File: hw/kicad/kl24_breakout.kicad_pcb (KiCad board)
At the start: 2 copper layers, 36.1 x 20.8 mm, 56 parts, among them J1 USB-micro-ab, J2 ARM_10PIN, P1 BATT+, P10 TST, P11 TST, P12 TST, P13 TST, P14 TST, P15 TST, P16 TST, P17 TST, P18 TST, P19 TST, P2 BATT-, P20 TST, P21 TST, P22 TST, P23 TST, P24 TST, P25 TST, P26 TST, P27 TST, P28 TST, P29 TST, P3 USB_V, P30 TST, P31 TST, P32 TST, P33 TST, P34 TST, P35 TST, P36 TST, P4 USB_GND, P5 TST, P6 TST, P7 TST, P8 TST, P9 TST, U1 MCP73831, U2 M25P05-A, U3 MKL24Z64VFM4, U4 LP3985, X1 CRYSTAL

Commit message: - add indicator led + resitor and jumper to pcb
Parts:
- added D3: LED, LED-0603, F.Cu at (150.2, 79.6)
- added JP1: JUMPER, jmp_small, F.Cu at (154.1, 82.2)
- added R5: 330, SM0603, F.Cu at (153.7, 77.0)
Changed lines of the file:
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@@
-(kicad_pcb (version 3) (host pcbnew "(2013-03-31 BZR 4008)-stable")
+(kicad_pcb (version 3) (host pcbnew "(2013-03-04 BZR 3984)-stable")
   (general
-    (links 88)
-    (no_connects 88)
+    (links 92)
+    (no_connects 92)
     (area 103.65685 49.41885 161.729444 95.639)
     (thickness 1.6)
@@
     (tracks 0)
     (zones 0)
-    (modules 56)
-    (nets 39)
+    (modules 59)
+    (nets 41)
   )
   (page A3)
@@
   (net 31 9)
   (net 32 LIPO+)
-  (net 33 N-0000044)
-  (net 34 N-0000045)
+  (net 33 N-0000043)
+  (net 34 N-0000044)
   (net 35 N-0000046)
-  (net 36 USB_DM)
-  (net 37 USB_DP)
-  (net 38 USB_VBUS)
+  (net 36 N-0000047)
+  (net 37 N-0000048)
+  (net 38 USB_DM)
+  (net 39 USB_DP)
+  (net 40 USB_VBUS)
   (net_class Default "This is the default net class."
     (clearance 0.254)
@@
     (add_net 9)
     (add_net LIPO+)
+    (add_net N-0000043)
     (add_net N-0000044)
-    (add_net N-0000045)
     (add_net N-0000046)
+    (add_net N-0000047)
+    (add_net N-0000048)
     (add_net USB_DM)
     (add_net USB_DP)
@@
     (pad 1 thru_hole circle (at 0 0) (size 1.75 1.75) (drill 1.02)
       (layers *.Cu *.Mask F.SilkS)
-      (net 38 USB_VBUS)
+      (net 40 USB_VBUS)
     )
   )
@@
     (pad 1 smd rect (at -0.762 0) (size 0.635 1.143)
       (layers F.Cu F.Paste F.Mask)
-      (net 33 N-0000044)
+      (net 35 N-0000046)
     )
     (pad 2 smd rect (at 0.762 0) (size 0.635 1.143)
@@
     (pad 1 smd rect (at -0.762 0) (size 0.635 1.143)
       (layers F.Cu F.Paste F.Mask)
-      (net 35 N-0000046)
+      (net 37 N-0000048)
     )
     (pad 2 smd rect (at 0.762 0) (size 0.635 1.143)
       (layers F.Cu F.Paste F.Mask)
-      (net 34 N-0000045)
+      (net 36 N-0000047)
     )
     (model smd\resistors\R0603.wrl
@@
     (pad 1 smd rect (at -0.762 0) (size 0.635 1.143)
       (layers F.Cu F.Paste F.Mask)
-      (net 37 USB_DP)
+      (net 39 USB_DP)
     )
     (pad 2 smd rect (at 0.762 0) (size 0.635 1.143)
@@
     (pad 1 smd rect (at -0.762 0) (size 0.635 1.143)
       (layers F.Cu F.Paste F.Mask)
-      (net 36 USB_DM)
+      (net 38 USB_DM)
     )
     (pad 2 smd rect (at 0.762 0) (size 0.635 1.143)
@@
     (pad 1 smd rect (at -0.762 0) (size 0.635 1.143)
       (layers F.Cu F.Paste F.Mask)
-      (net 38 USB_VBUS)
+      (net 40 USB_VBUS)
     )
     (pad 2 smd rect (at 0.762 0) (size 0.635 1.143)
@@
     (pad 1 smd rect (at -0.762 0) (size 0.635 1.143)
       (layers F.Cu F.Paste F.Mask)
-      (net 38 USB_VBUS)
+      (net 40 USB_VBUS)
     )
     (pad 2 smd rect (at 0.762 0) (size 0.635 1.143)
@@
     (pad 1 smd rect (at -0.762 0) (size 0.635 1.143)
       (layers F.Cu F.Paste F.Mask)
-      (net 38 USB_VBUS)
+      (net 40 USB_VBUS)
     )
     (pad 2 smd rect (at 0.762 0) (size 0.635 1.143)
       (layers F.Cu F.Paste F.Mask)
-      (net 35 N-0000046)
+      (net 37 N-0000048)
     )
     (model smd\resistors\R0603.wrl
@@
     (pad 2 smd rect (at 0.762 0) (size 0.635 1.143)
       (layers F.Cu F.Paste F.Mask)
-      (net 38 USB_VBUS)
+      (net 40 USB_VBUS)
     )
     (model smd\resistors\R0603.wrl
@@
     (pad 1 smd rect (at 0 0) (size 0.55 1)
       (layers F.Cu F.Paste F.Mask)
-      (net 34 N-0000045)
+      (net 36 N-0000047)
     )
     (pad 2 smd rect (at 0.95 0) (size 0.55 1)
@@
     (pad 4 smd rect (at 1.9 -2.7) (size 0.55 1)
       (layers F.Cu F.Paste F.Mask)
-      (net 38 USB_VBUS)
+      (net 40 USB_VBUS)
     )
     (pad 5 smd rect (at 0 -2.7) (size 0.55 1)
       (layers F.Cu F.Paste F.Mask)
-      (net 33 N-0000044)
+      (net 35 N-0000046)
     )
   )
@@
     (pad 1 smd rect (at 0 0) (size 0.6 1.1)
       (layers F.Cu F.Paste F.Mask)
-      (net 38 USB_VBUS)
+      (net 40 USB_VBUS)
     )
     (pad 2 smd rect (at 0.95 0) (size 0.6 1.1)
@@
     (pad 3 smd rect (at 1.9 0) (size 0.6 1.1)
       (layers F.Cu F.Paste F.Mask)
-      (net 38 USB_VBUS)
+      (net 40 USB_VBUS)
     )
     (pad 4 smd rect (at 1.9 -2.8) (size 0.6 1.1)
@@
     (pad 1 smd rect (at -1.3 -2.85 270) (size 0.4 1.4)
       (layers F.Cu F.Paste F.Mask)
-      (net 38 USB_VBUS)
+      (net 40 USB_VBUS)
     )
     (pad 2 smd rect (at -0.65 -2.85 270) (size 0.4 1.4)
       (layers F.Cu F.Paste F.Mask)
-      (net 36 USB_DM)
+      (net 38 USB_DM)
     )
     (pad 3 smd rect (at 0 -2.85 270) (size 0.4 1.4)
       (layers F.Cu F.Paste F.Mask)
-      (net 37 USB_DP)
+      (net 39 USB_DP)
     )
     (pad 4 smd rect (at 0.65 -2.85 270) (size 0.4 1.4)
@@
     )
   )
+  (module SM0603 (layer F.Cu)
+    (at 153.67 76.962)
+    (attr smd)
+    (fp_text reference R5 (at 0 0) (layer F.SilkS)
+      (effects (font (size 0.508 0.4572) (thickness 0.1143)))
+    )
+    (fp_text value 330 (at 0 0) (layer F.SilkS) hide
+      (effects (font (size 0.508 0.4572) (thickness 0.1143)))
+    )
+    (fp_line (start -1.143 -0.635) (end 1.143 -0.635) (layer F.SilkS) (width 0.127))
+    (fp_line (start 1.143 -0.635) (end 1.143 0.635) (layer F.SilkS) (width 0.127))
+    (fp_line (start 1.143 0.635) (end -1.143 0.635) (layer F.SilkS) (width 0.127))
+    (fp_line (start -1.143 0.635) (end -1.143 -0.635) (layer F.SilkS) (width 0.127))
+    (pad 1 smd rect (at -0.762 0) (size 0.635 1.143)
+      (layers F.Cu F.Paste F.Mask)
+      (net 34 N-0000044)
+    )
+    (pad 2 smd rect (at 0.762 0) (size 0.635 1.143)
+      (layers F.Cu F.Paste F.Mask)
+      (net 12 2)
+    )
+    (model smd\resistors\R0603.wrl
+      (at (xyz 0 0 0.001))
+      (scale (xyz 0.5 0.5 0.5))
+      (rotate (xyz 0 0 0))
+    )
+  )
+  (module LED-0603 (layer F.Cu)
+    (at 150.241 79.629)
+    (descr "LED 0603 smd package")
+    (tags "LED led 0603 SMD smd SMT smt smdled SMDLED smtled SMTLED")
+    (attr smd)
+    (fp_text reference D3 (at 0 -1.016) (layer F.SilkS)
+      (effects (font (size 0.508 0.508) (thickness 0.127)))
+    )
+    (fp_text value LED (at 0 1.016) (layer F.SilkS)
+      (effects (font (size 0.508 0.508) (thickness 0.127)))
+    )
+    (fp_line (start 0.44958 -0.44958) (end 0.44958 0.44958) (layer F.SilkS) (width 0.06604))
+    (fp_line (start 0.44958 0.44958) (end 0.84836 0.44958) (layer F.SilkS) (width 0.06604))
+    (fp_line (start 0.84836 -0.44958) (end 0.84836 0.44958) (layer F.SilkS) (width 0.06604))
+    (fp_line (start 0.44958 -0.44958) (end 0.84836 -0.44958) (layer F.SilkS) (width 0.06604))
+    (fp_line (start -0.84836 -0.44958) (end -0.84836 0.44958) (layer F.SilkS) (width 0.06604))
+    (fp_line (start -0.84836 0.44958) (end -0.44958 0.44958) (layer F.SilkS) (width 0.06604))
+    (fp_line (start -0.44958 -0.44958) (end -0.44958 0.44958) (layer F.SilkS) (width 0.06604))
+    (fp_line (start -0.84836 -0.44958) (end -0.44958 -0.44958) (layer F.SilkS) (width 0.06604))
+    (fp_line (start 0 -0.44958) (end 0 -0.29972) (layer F.SilkS) (width 0.06604))
+    (fp_line (start 0 -0.29972) (end 0.29972 -0.29972) (layer F.SilkS) (width 0.06604))
+    (fp_line (start 0.29972 -0.44958) (end 0.29972 -0.29972) (layer F.SilkS) (width 0.06604))
+    (fp_line (start 0 -0.44958) (end 0.29972 -0.44958) (layer F.SilkS) (width 0.06604))
+    (fp_line (start 0 0.29972) (end 0 0.44958) (layer F.SilkS) (width 0.06604))
+    (fp_line (start 0 0.44958) (end 0.29972 0.44958) (layer F.SilkS) (width 0.06604))
+    (fp_line (start 0.29972 0.29972) (end 0.29972 0.44958) (layer F.SilkS) (width 0.06604))
+    (fp_line (start 0 0.29972) (end 0.29972 0.29972) (layer F.SilkS) (width 0.06604))
+    (fp_line (start 0 -0.14986) (end 0 0.14986) (layer F.SilkS) (width 0.06604))
+    (fp_line (start 0 0.14986) (end 0.29972 0.14986) (layer F.SilkS) (width 0.06604))
+    (fp_line (start 0.29972 -0.14986) (end 0.29972 0.14986) (layer F.SilkS) (width 0.06604))
+    (fp_line (start 0 -0.14986) (end 0.29972 -0.14986) (layer F.SilkS) (width 0.06604))
+    (fp_line (start 0.44958 -0.39878) (end -0.44958 -0.39878) (layer F.SilkS) (width 0.1016))
+    (fp_line (start 0.44958 0.39878) (end -0.44958 0.39878) (layer F.SilkS) (width 0.1016))
+    (pad 1 smd rect (at -0.7493 0) (size 0.79756 0.79756)
+      (layers F.Cu F.Paste F.Mask)
+      (net 33 N-0000043)
+    )
+    (pad 2 smd rect (at 0.7493 0) (size 0.79756 0.79756)
+      (layers F.Cu F.Paste F.Mask)
+      (net 34 N-0000044)
+    )
+  )
+  (module jmp_small (layer F.Cu)
+    (at 154.051 82.169)
+    (fp_text reference JP1 (at 0 -2.032) (layer F.SilkS)
+      (effects (font (size 1 1) (thickness 0.15)))
+    )
+    (fp_text value JUMPER (at 0 1.9) (layer F.SilkS)
+      (effects (font (size 1 1) (thickness 0.15)))
+    )
+    (pad 1 smd trapezoid (at 0 -0.635) (size 1 1) (rect_delta 0 0.25 )
+      (layers F.Cu F.Paste F.Mask)
+      (net 13 20)
+    )
+    (pad 2 smd trapezoid (at 0 0.635) (size 1 1) (rect_delta 0 -0.25 )
+      (layers F.Cu F.Paste F.Mask)
+      (net 33 N-0000043)
+    )
+  )

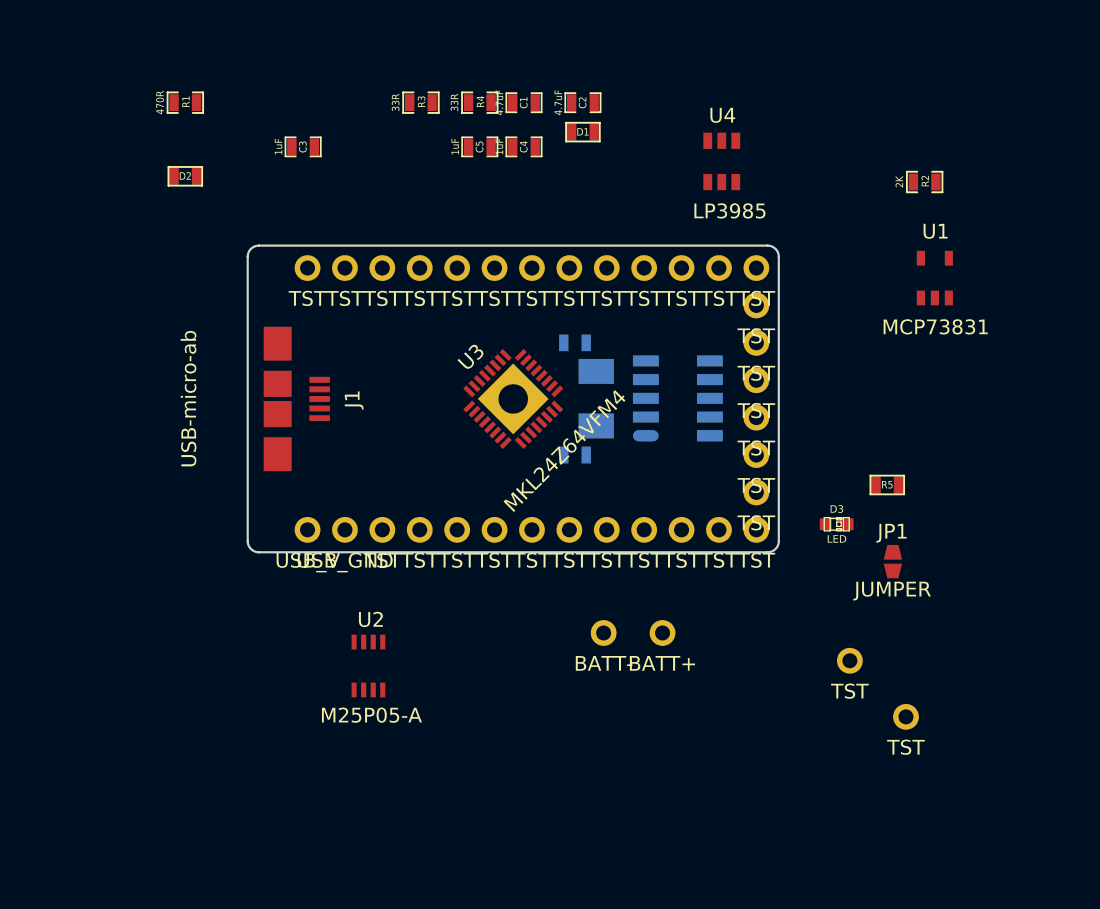
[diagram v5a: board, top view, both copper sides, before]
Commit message: - update pcb with new netlist
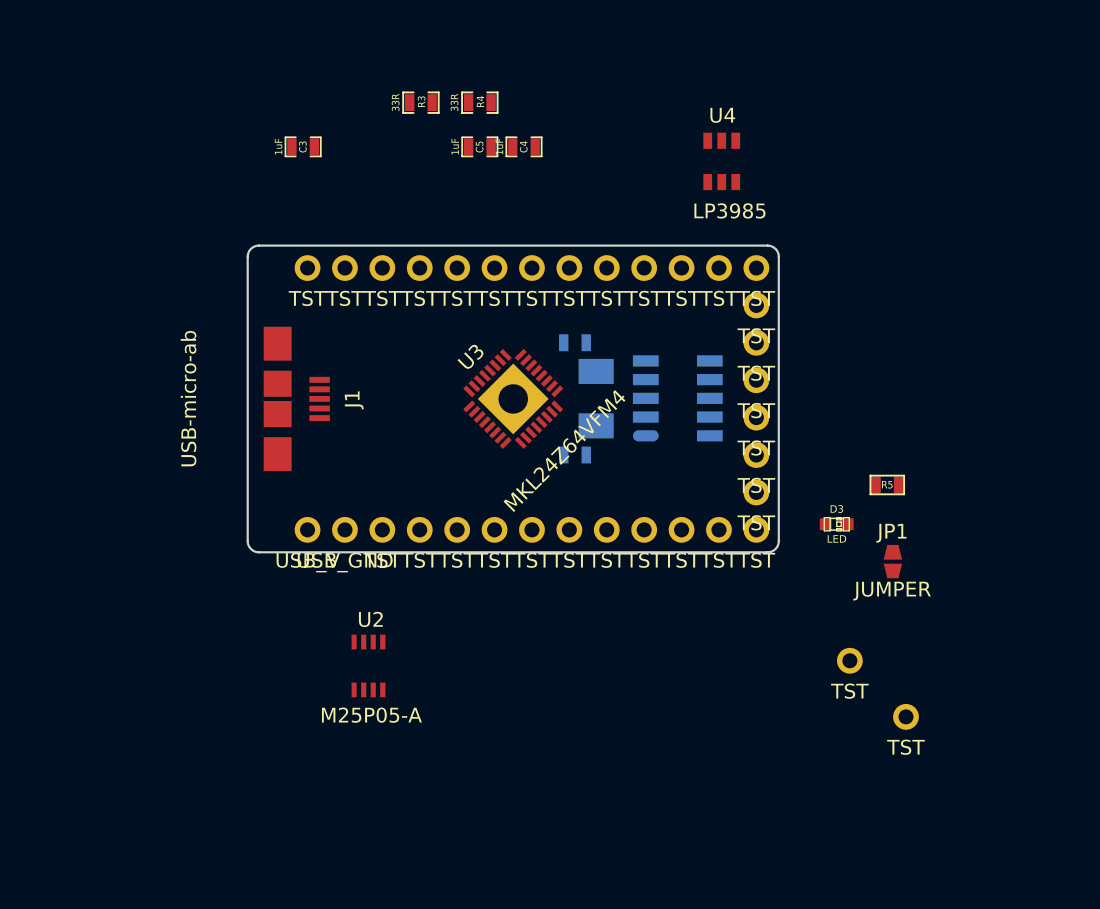
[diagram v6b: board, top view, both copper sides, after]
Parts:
- removed C1, C2: 4.7uF, SM0603_Capa
- removed D1: LED, SM0603
- removed D2: DIODESCH, SM0603
- removed P1: BATT+, TEST_0.100
- removed P2: BATT-, TEST_0.100
- removed R1: 470R, SM0603_Resistor
- removed R2: 2K, SM0603_Resistor
- removed U1: MCP73831, MCP73831

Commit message: fix up a bit
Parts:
- removed C5: 1uF, SM0603_Capa
- removed C6, C7: 22pF, SM0603_Capa
- removed D3: LED, LED-0603
- removed J2: ARM_10PIN, ARM_10_PIN_SMT
- removed R5: 330, SM0603
- removed U3: MKL24Z64VFM4, MKL24Z64VFM4
- removed U4: LP3985, MCP1640
- added C1: 22pF, SM0603, F.Cu at (135.9, 89.7)
- added C2: 22pF, SM0603, F.Cu at (138.4, 92.7)
- added D1: LED, LED-0603, F.Cu at (125.0, 84.6)
- added P1: TST, TEST_0.100, F.Cu at (109.2, 87.4)
- added P2: TST, TEST_0.100, F.Cu at (119.6, 86.1)
- added P37: SWCLK, TEST_0.100, F.Cu at (130.0, 97.5)
- added P38: NRESET, TEST_0.100, F.Cu at (124.0, 100.6)
- added P39: SWD_GND, TEST_0.100, F.Cu at (139.4, 98.0)
- added R1: 33R, SM0603, F.Cu at (129.0, 86.4)
- added R2: 33R, SM0603, F.Cu at (133.1, 89.2)
- added U1: MKL24Z64VFM4, MKL24Z64VFM4, F.Cu at (129.5, 71.1)
- C3, C4: footprint SM0603_Capa -> SM0603
- P3: value USB_V -> TST
- P33: value TST -> USB_V
- P34: value TST -> USB_GND
- P35: value TST -> SWD_VCC
- P36: value TST -> SWDIO
- P4: value USB_GND -> TST
- R3, R4: value 33R -> 330; footprint SM0603_Resistor -> SM0603
- U2: value M25P05-A -> LP3985; footprint TSSOP-8 -> LP3985
- moved R4 42.7 mm to (134.1, 93.0)
- moved R3 40.5 mm to (124.2, 91.4)
- moved C3 37.1 mm to (133.9, 85.3)
- moved P35 35.1 mm to (119.9, 93.2)
- moved C4 34.8 mm to (123.7, 88.4)
- moved P36 24.6 mm to (126.5, 88.1)
- moved U2 21.9 mm to (140.0, 86.4)
- moved JP1 17.5 mm to (137.2, 86.6)
- moved P34 15.2 mm to (99.3, 64.8)
- moved P33 13.5 mm to (103.4, 63.0)
- moved P3 6.62 mm to (113.8, 86.6)
- moved P22 5.08 mm to (139.7, 62.2)
- moved P23 5.08 mm to (137.2, 62.2)
- moved P26 5.08 mm to (129.5, 62.2)
- moved P27 5.08 mm to (127.0, 62.2)
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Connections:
- C3 pad 1: 3.3V_SUPPLY -> USB_VBUS
- C3 pad 2: 2 -> 8
- C4 pad 1: USB_VBUS -> 7
- C4 pad 2: 2 -> 8
- J1 pad 4: (no net) -> Net-<J1-Pad4>
- J1 pad 5: 2 -> 8
- J1 pad 6: 2 -> 8
- JP1 pad 2: N-0000040 -> Net-<D1-Pad1>
- P10 pad 1: 6 -> 10
- P11 pad 1: 3.3V_SUPPLY -> 11
- P12 pad 1: 2 -> 12
- P13 pad 1: 9 -> 13
- P14 pad 1: 10 -> 14
- P15 pad 1: 11 -> 15
- P16 pad 1: 12 -> 16
- P17 pad 1: 13 -> 17
- P18 pad 1: 14 -> 18
- P19 pad 1: 15 -> 19
- P20 pad 1: 16 -> 20
- P21 pad 1: 17 -> 21
- P22 pad 1: 18 -> 22
- P23 pad 1: 19 -> 23
- P24 pad 1: 20 -> 24
- P25 pad 1: 21 -> 25
- P26 pad 1: 22 -> 26
- P27 pad 1: 23 -> 27
- P28 pad 1: 24 -> 28
- P29 pad 1: 25 -> 29
- P3 pad 1: USB_VBUS -> 3
- P30 pad 1: 26 -> 30
- P31 pad 1: 27 -> 31
- P32 pad 1: 28 -> 32
- P33 pad 1: 29 -> USB_VBUS
- P34 pad 1: 30 -> 8
- P35 pad 1: 31 -> 7
- P36 pad 1: 32 -> 13
- P4 pad 1: 2 -> 4
- P5 pad 1: 1 -> 5
- P6 pad 1: 2 -> 6
- P7 pad 1: 3 -> 7
- P8 pad 1: 4 -> 8
- P9 pad 1: 5 -> 9
- R3 pad 1: USB_DP -> Net-<J1-Pad4>
- R3 pad 2: 3 -> 20
- R4 pad 1: USB_DM -> Net-<D1-Pad2>
- R4 pad 2: 4 -> 8
- U2 pad 1: 25 -> USB_VBUS
- U2 pad 2: 28 -> 8
- U2 pad 3: (no net) -> USB_VBUS
- U2 pad 4: 2 -> Net-<U2-Pad4>
- U2 pad 5: 27 -> 7

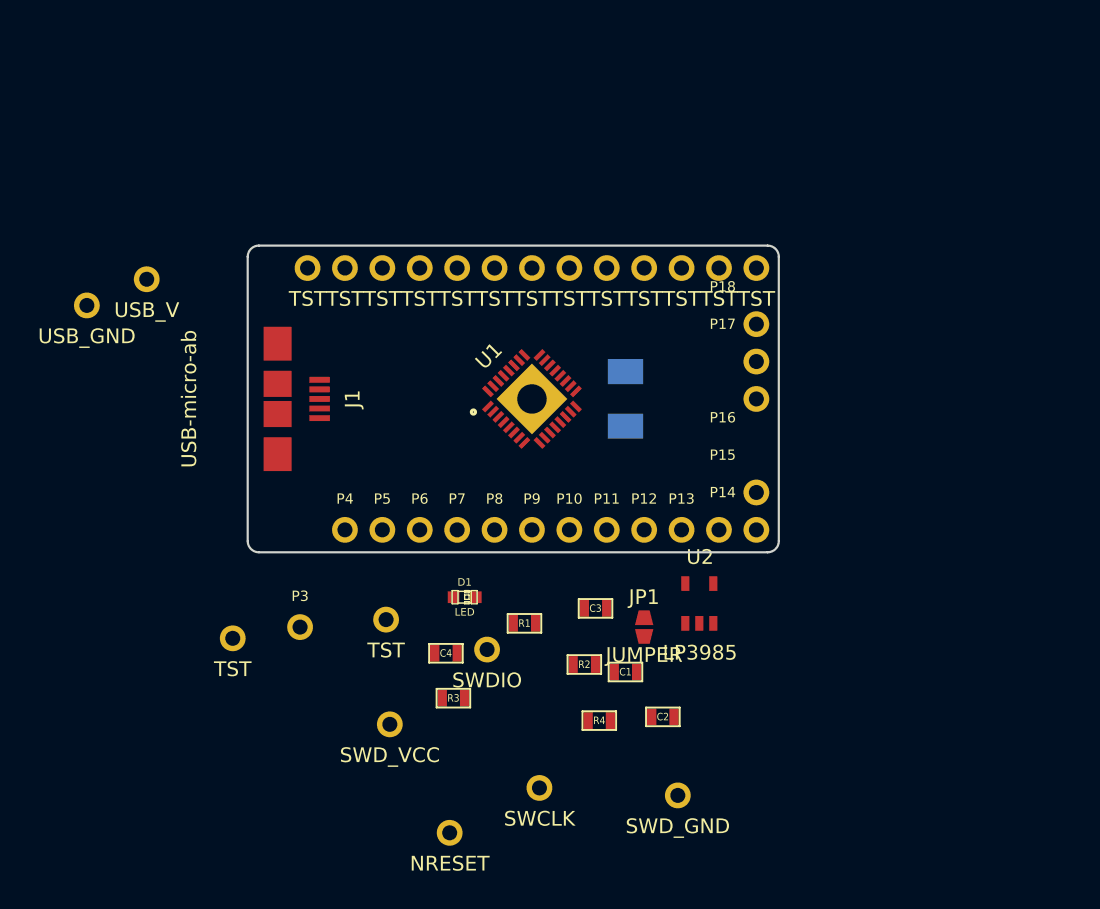
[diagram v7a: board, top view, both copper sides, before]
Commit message: fix some pcb labels
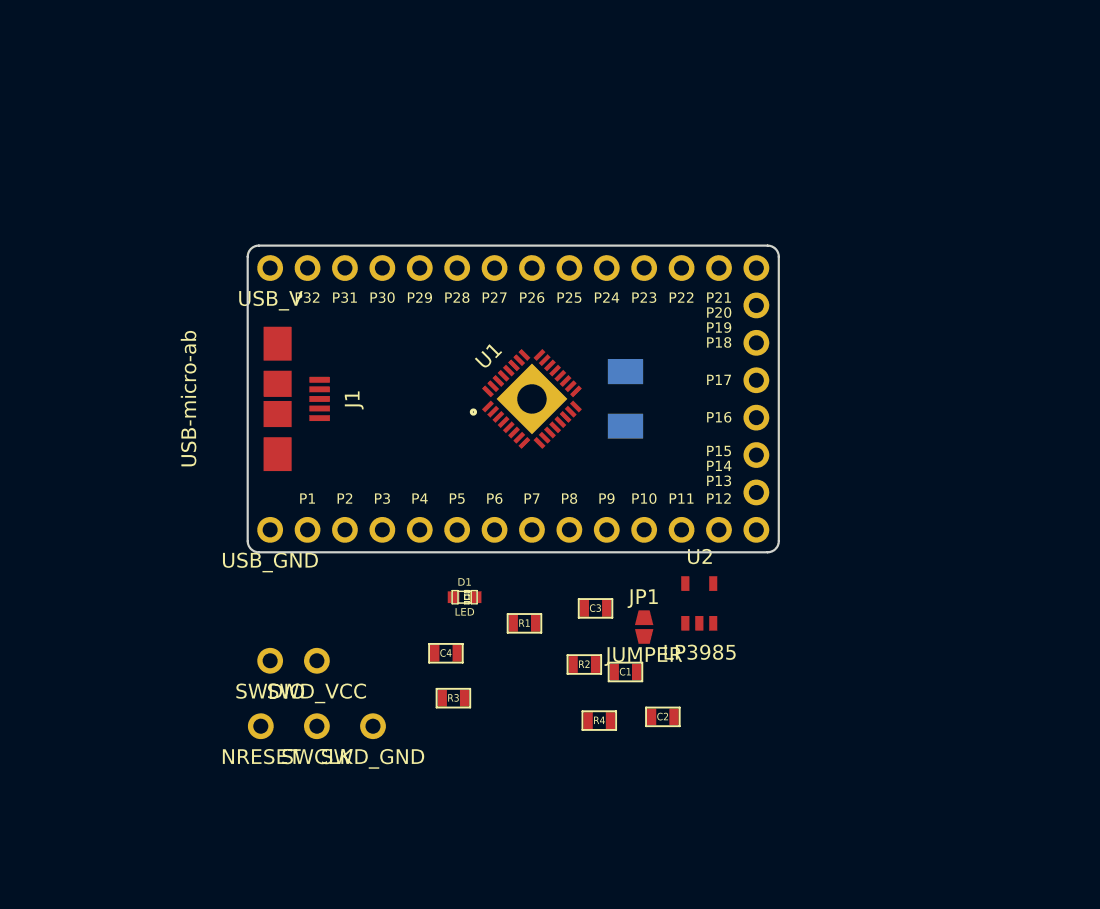
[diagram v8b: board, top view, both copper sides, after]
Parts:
- moved P39 21.2 mm to (118.7, 93.3)
- moved P34 19.7 mm to (111.8, 80.0)
- moved P37 15.7 mm to (114.9, 93.3)
- moved P36 14.8 mm to (111.8, 88.9)
- moved P38 14.7 mm to (111.1, 93.3)
- moved P1 8.95 mm to (114.3, 80.0)
- moved P3 8.65 mm to (119.4, 80.0)
- moved P33 8.42 mm to (111.8, 62.2)
- moved P2 6.71 mm to (116.8, 80.0)
- moved P35 6.57 mm to (114.9, 88.9)
- moved P12 5.08 mm to (142.2, 80.0)
- moved P13 5.08 mm to (144.8, 80.0)
- moved P8 5.08 mm to (132.1, 80.0)
- moved P9 5.08 mm to (134.6, 80.0)
- moved P15 5.08 mm to (144.8, 74.9)
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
